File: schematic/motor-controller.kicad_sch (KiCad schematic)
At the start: 11 parts, among them J1 Raspberry_Pi_4, M1 Motor_DC, M2 Motor_DC, SW1 SW_SPST, SW2 RotaryEncoder, SW3 RotaryEncoder, U1 L298N, U2 PCA9306, U3 LM2596S-5

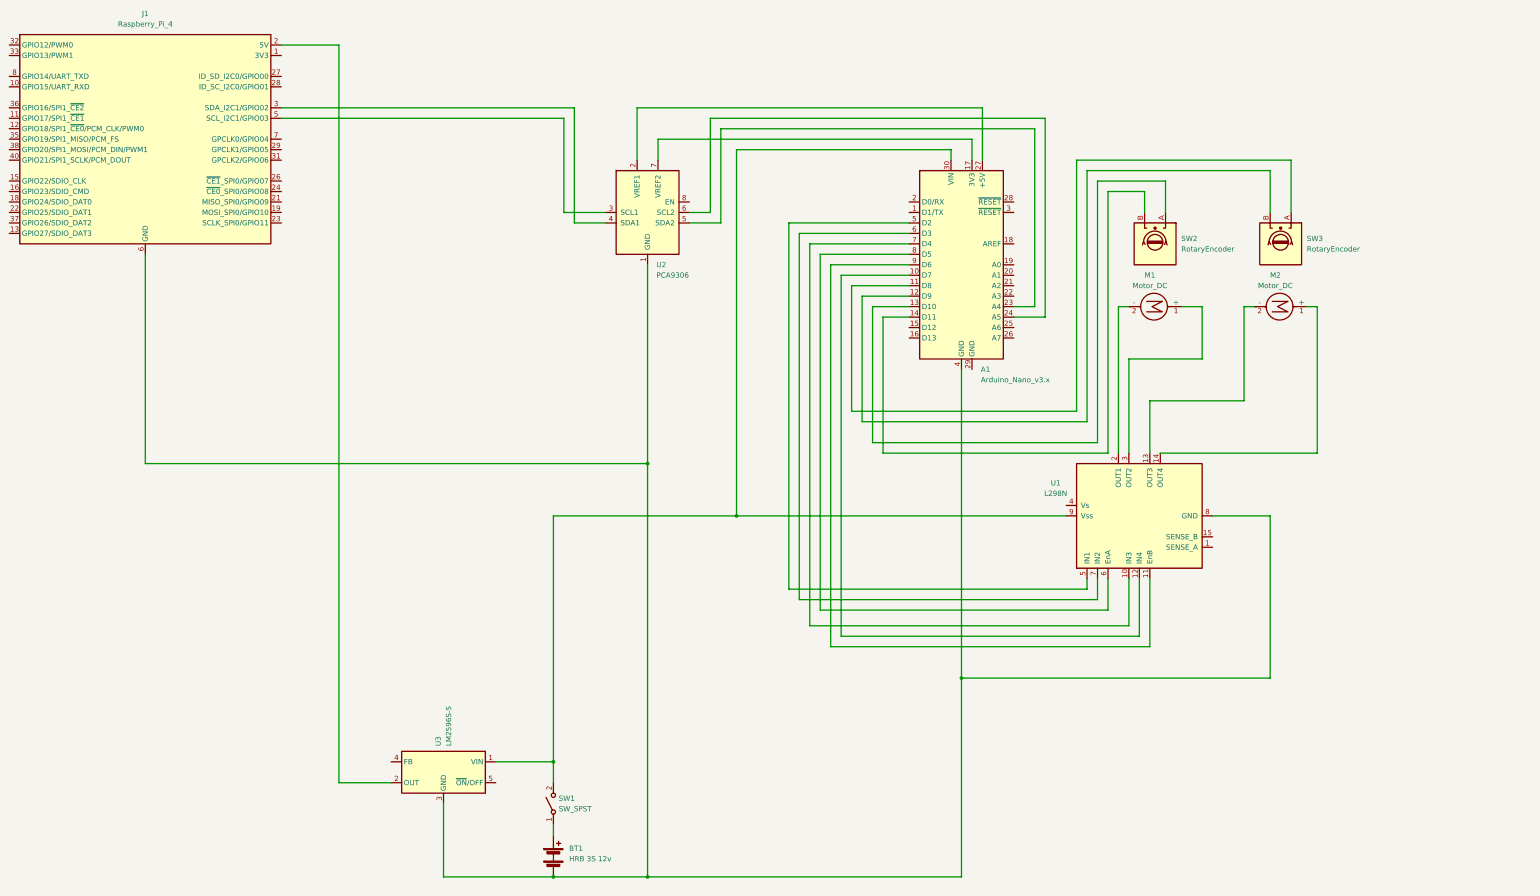
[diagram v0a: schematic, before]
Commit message: Схема подключения моторов, ардуино, RPI (I2c)
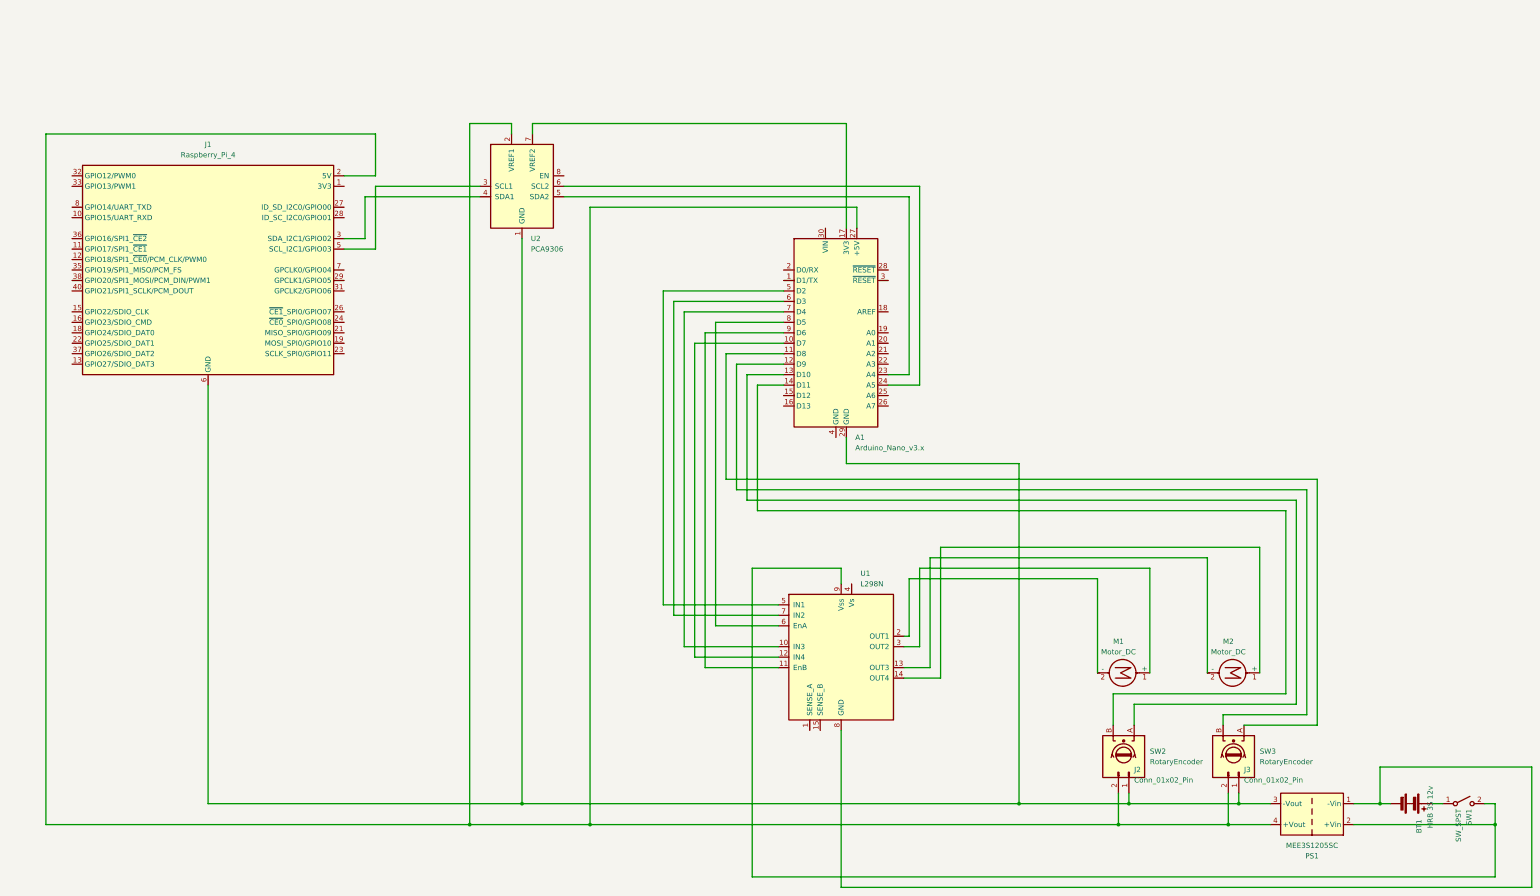
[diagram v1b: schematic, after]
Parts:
- removed U3: LM2596S-5, Package_TO_SOT_SMD:TO-263-5_TabPin3, symbol Regulator_Switching:LM2596S-5
- added J2, J3: Conn_01x02_Pin, symbol Connector:Conn_01x02_Pin
- added PS1: MEE3S1205SC, Converter_DCDC:Converter_DCDC_Murata_MEE3SxxxxSC_THT, symbol Converter_DCDC:MEE3S1205SC
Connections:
- net at SW1.2 (B), U1.9 (Vss): now also PS1.2 (+Vin); no longer A1.30 (VIN)
- net at J1.2 (5V), J1.4 (5V): now also A1.27 (+5V), U2.2 (VREF1), J2.2 (Pin_2), J3.2 (Pin_2), PS1.4 (+Vout)
- net at J1.14 (GND), J1.20 (GND), J1.25 (GND)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: now also A1.29 (GND), J2.1 (Pin_1), J3.1 (Pin_1), PS1.3 (-Vout); no longer A1.4 (GND), BT1.2 (-), U1.8 (GND)
- new net: BT1.2 (-), PS1.1 (-Vin), U1.8 (GND)
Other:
- moved on the sheet: A1, BT1, J1, M1, M2, SW1, SW2, SW3, U1, U2

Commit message: Logic level converter fix
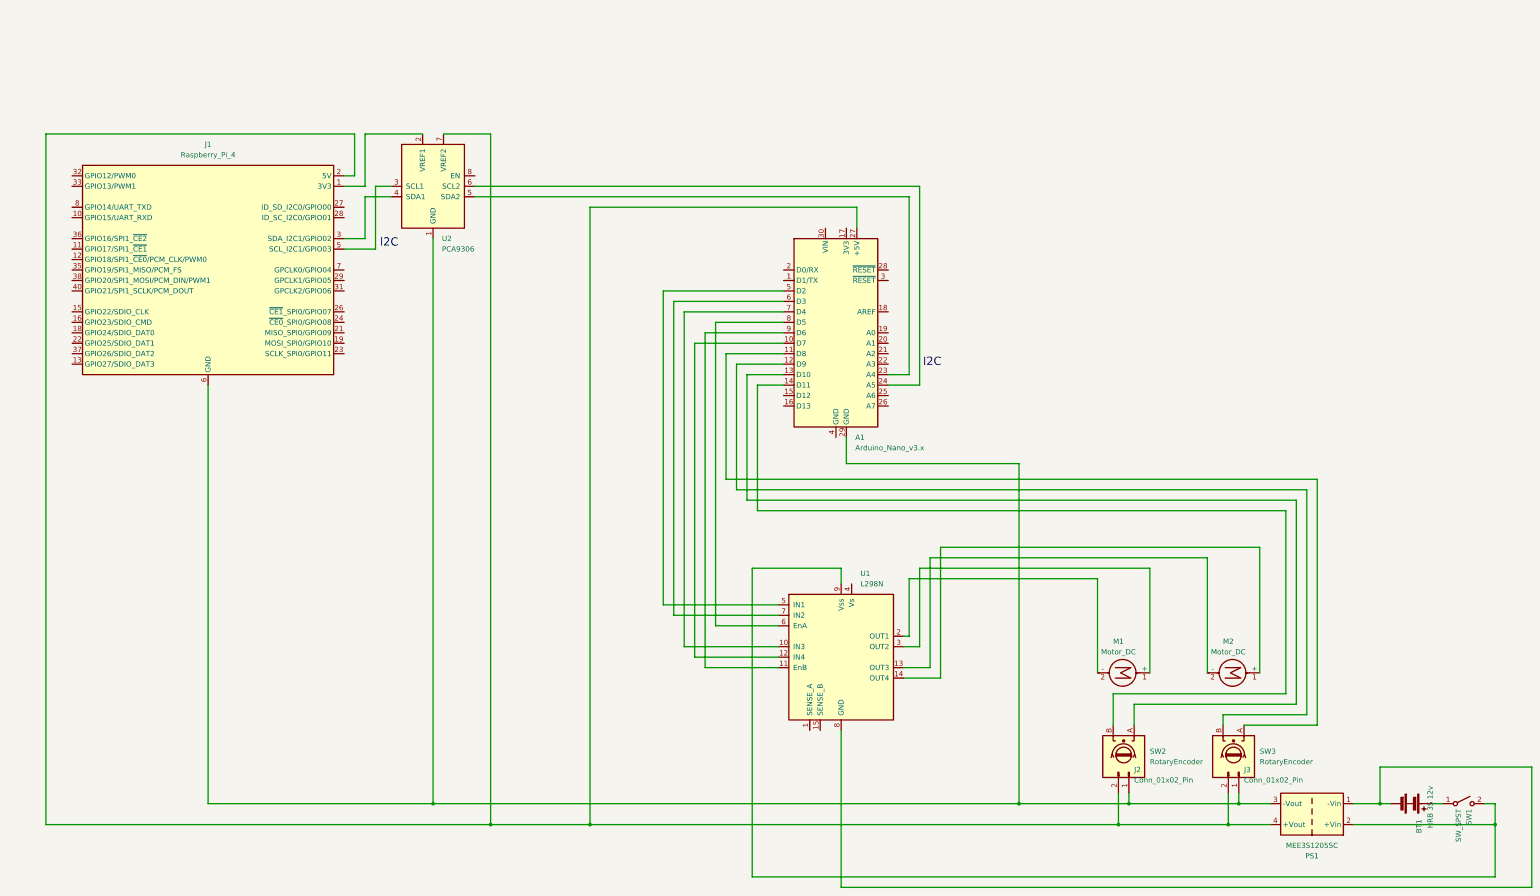
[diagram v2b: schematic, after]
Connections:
- net at A1.27 (+5V), J1.2 (5V), J1.4 (5V)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: now also U2.7 (VREF2); no longer U2.2 (VREF1)
- net at J1.1 (3V3), J1.17 (3V3): now also U2.2 (VREF1)
- net at A1.17 (3V3): no longer U2.7 (VREF2)
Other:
- note added: "I2C"
- moved on the sheet: U2
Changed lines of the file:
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@@
 	(generator_version "9.0")
 	(paper "A3")
+	(text "I2C"
+		(exclude_from_sim no)
+		(at 254.508 103.632 0)
+		(effects
+			(font
+				(size 2 2)
+				(thickness 0.25)
+			)
+		)
+	)
+	(text "I2C"
+		(exclude_from_sim no)
+		(at 122.682 74.676 0)
+		(effects
+			(font
+				(size 2 2)
+				(thickness 0.25)
+			)
+		)
+	)
+	(junction
+		(at 147.32 215.9)
+		(diameter 0)
+		(color 0 0 0 0)
+	)
 	(junction
 		(at 326.39 215.9)
@@
 	)
 	(junction
-		(at 142.24 215.9)
-		(diameter 0)
-		(color 0 0 0 0)
-	)
-	(junction
-		(at 154.94 210.82)
+		(at 133.35 210.82)
 		(diameter 0)
 		(color 0 0 0 0)
@@
 	(wire
 		(pts
-			(xy 165.1 63.5) (xy 248.92 63.5)
+			(xy 143.51 63.5) (xy 248.92 63.5)
 		)
 		(stroke
@@
 	(wire
 		(pts
-			(xy 233.68 71.12) (xy 233.68 45.72)
+			(xy 116.84 48.26) (xy 116.84 60.96)
 		)
 		(stroke
@@
 	(wire
 		(pts
-			(xy 39.37 215.9) (xy 142.24 215.9)
+			(xy 116.84 48.26) (xy 130.81 48.26)
+		)
+		(stroke
+			(width 0)
+			(type default)
+		)
+	)
+	(wire
+		(pts
+			(xy 39.37 215.9) (xy 147.32 215.9)
 		)
 		(stroke
@@
 	(wire
 		(pts
-			(xy 119.38 58.42) (xy 111.76 58.42)
+			(xy 114.3 58.42) (xy 111.76 58.42)
 		)
 		(stroke
@@
 	(wire
 		(pts
-			(xy 154.94 73.66) (xy 154.94 210.82)
+			(xy 133.35 73.66) (xy 133.35 210.82)
 		)
 		(stroke
@@
 	(wire
 		(pts
-			(xy 119.38 48.26) (xy 39.37 48.26)
+			(xy 114.3 48.26) (xy 39.37 48.26)
 		)
 		(stroke
@@
 	(wire
 		(pts
-			(xy 116.84 63.5) (xy 144.78 63.5)
+			(xy 116.84 63.5) (xy 123.19 63.5)
 		)
 		(stroke
@@
 	(wire
 		(pts
-			(xy 142.24 45.72) (xy 142.24 215.9)
-		)
-		(stroke
-			(width 0)
-			(type default)
-		)
-	)
-	(wire
-		(pts
-			(xy 233.68 45.72) (xy 157.48 45.72)
+			(xy 147.32 48.26) (xy 147.32 215.9)
 		)
 		(stroke
@@
 	(wire
 		(pts
+			(xy 111.76 60.96) (xy 116.84 60.96)
+		)
+		(stroke
+			(width 0)
+			(type default)
+		)
+	)
+	(wire
+		(pts
 			(xy 388.62 210.82) (xy 391.16 210.82)
 		)
@@
 	(wire
 		(pts
-			(xy 119.38 60.96) (xy 144.78 60.96)
+			(xy 147.32 215.9) (xy 171.45 215.9)
+		)
+		(stroke
+			(width 0)
+			(type default)
+		)
+	)
+	(wire
+		(pts
+			(xy 119.38 60.96) (xy 123.19 60.96)
 		)
 		(stroke
@@
 	(wire
 		(pts
-			(xy 152.4 45.72) (xy 152.4 48.26)
-		)
-		(stroke
-			(width 0)
-			(type default)
-		)
-	)
-	(wire
-		(pts
 			(xy 210.82 228.6) (xy 210.82 153.67)
 		)
@@
 	(wire
 		(pts
-			(xy 119.38 48.26) (xy 119.38 58.42)
+			(xy 114.3 48.26) (xy 114.3 58.42)
 		)
 		(stroke
@@
 	(wire
 		(pts
-			(xy 78.74 210.82) (xy 154.94 210.82)
+			(xy 78.74 210.82) (xy 133.35 210.82)
 		)
 		(stroke
@@
 	(wire
 		(pts
+			(xy 133.35 210.82) (xy 275.59 210.82)
+		)
+		(stroke
+			(width 0)
+			(type default)
+		)
+	)
+	(wire
+		(pts
 			(xy 251.46 109.22) (xy 251.46 60.96)
 		)
@@
 	(wire
 		(pts
-			(xy 142.24 215.9) (xy 171.45 215.9)
-		)
-		(stroke
-			(width 0)
-			(type default)
-		)
-	)
-	(wire
-		(pts
 			(xy 356.87 215.9) (xy 391.16 215.9)
 		)
@@
 	(wire
 		(pts
-			(xy 165.1 60.96) (xy 251.46 60.96)
+			(xy 143.51 60.96) (xy 251.46 60.96)
 		)
 		(stroke
@@
 	(wire
 		(pts
-			(xy 152.4 45.72) (xy 142.24 45.72)
-		)
-		(stroke
-			(width 0)
-			(type default)
-		)
-	)
-	(wire
-		(pts
-			(xy 154.94 210.82) (xy 275.59 210.82)
+			(xy 135.89 48.26) (xy 147.32 48.26)
 		)
 		(stroke
@@
 		(pts
 			(xy 210.82 228.6) (xy 391.16 228.6)
-		)
-		(stroke
-			(width 0)
-			(type default)
-		)
-	)
-	(wire
-		(pts
-			(xy 157.48 45.72) (xy 157.48 48.26)
 		)
 		(stroke
@@
 	(symbol
 		(lib_id "Interface:PCA9306")
-		(at 154.94 60.96 0)
+		(at 133.35 60.96 0)
 		(unit 1)
 		(exclude_from_sim no)
@@
 		(fields_autoplaced yes)
 		(property "Reference" "U2"
-			(at 157.0833 73.66 0)
+			(at 135.4933 73.66 0)
 			(effects
 				(font
@@
 		)
 		(property "Value" "PCA9306"
-			(at 157.0833 76.2 0)
+			(at 135.4933 76.2 0)
 			(effects
 				(font
@@
 		)
 		(property "Footprint" ""
-			(at 144.78 52.07 0)
+			(at 123.19 52.07 0)
 			(effects
 				(font
@@
 		)
 		(property "Datasheet" "http://www.ti.com/lit/ds/symlink/pca9306.pdf"
-			(at 147.32 49.53 0)
+			(at 125.73 49.53 0)
 			(effects
 				(font
@@
 		)
 		(property "Description" "Dual bidirectional I2C Bus and SMBus voltage level translator"
-			(at 154.94 60.96 0)
-			(effects
-				(font
+			(at 133.35 60.96 0)
+			(effects
+				(font
